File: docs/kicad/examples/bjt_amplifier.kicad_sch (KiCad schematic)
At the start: 18 parts, among them Q1 2N3904, Q2 2N3904

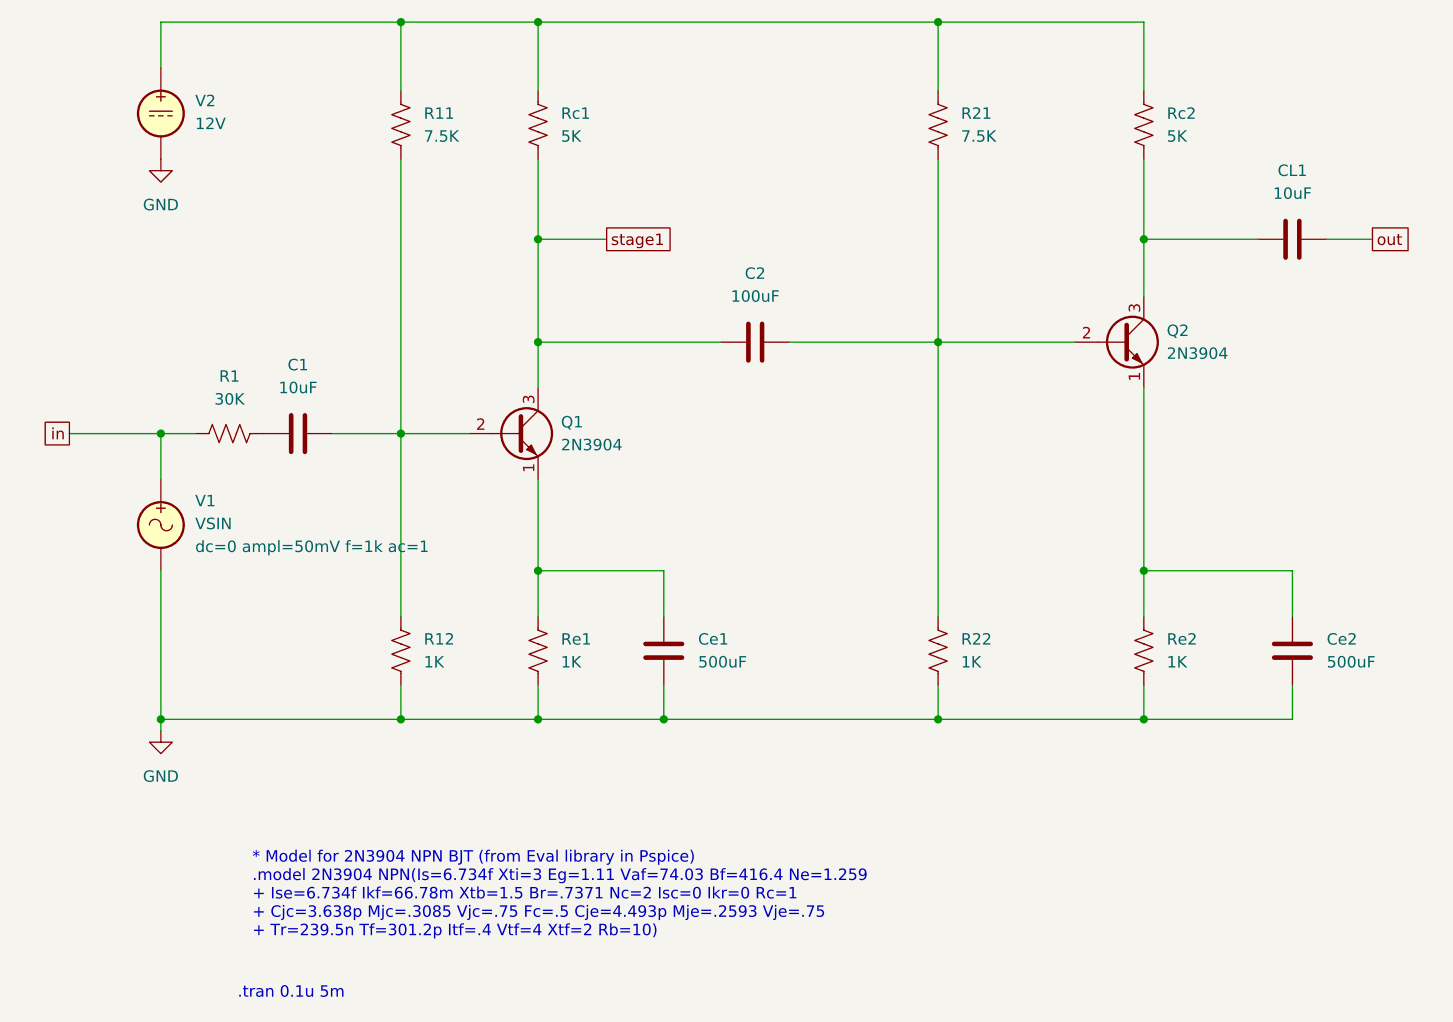
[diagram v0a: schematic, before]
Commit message: fix: file watcher polling, cross-probe removal, guide updates
- Rewrite file watcher from QFileSystemWatcher to mtime polling (KiCad's
  rename-over atomic save silently breaks QFileSystemWatcher tracking)
- Replace "Simulate Now" with "Re-Watch" button (resumes watching after Stop)
- Remove cross-probe/back-annotation from menu and docs (KiCad's cross-probe
  channel is private Eeschema-PcbNew, not an external API)
- Document cross-probe as known limitation in user guide
- Rename back_annotate.kicad_sch to bjt_amplifier.kicad_sch
- Make all Help dialogs non-modal (show() instead of exec())
- Add Help > KiCad User Guide entry with pre-built HTML
- Persist traces across KiCad re-simulations
- Add raw_ok check in bridge.simulate() (ngspice can exit 0 without writing .raw)
- Fix _panel_grid -> panel_grid typo in cross-probe helper
- Initialize all KiCad-related instance attributes

Co-Authored-By: Claude Opus 4.7 <noreply@anthropic.com>
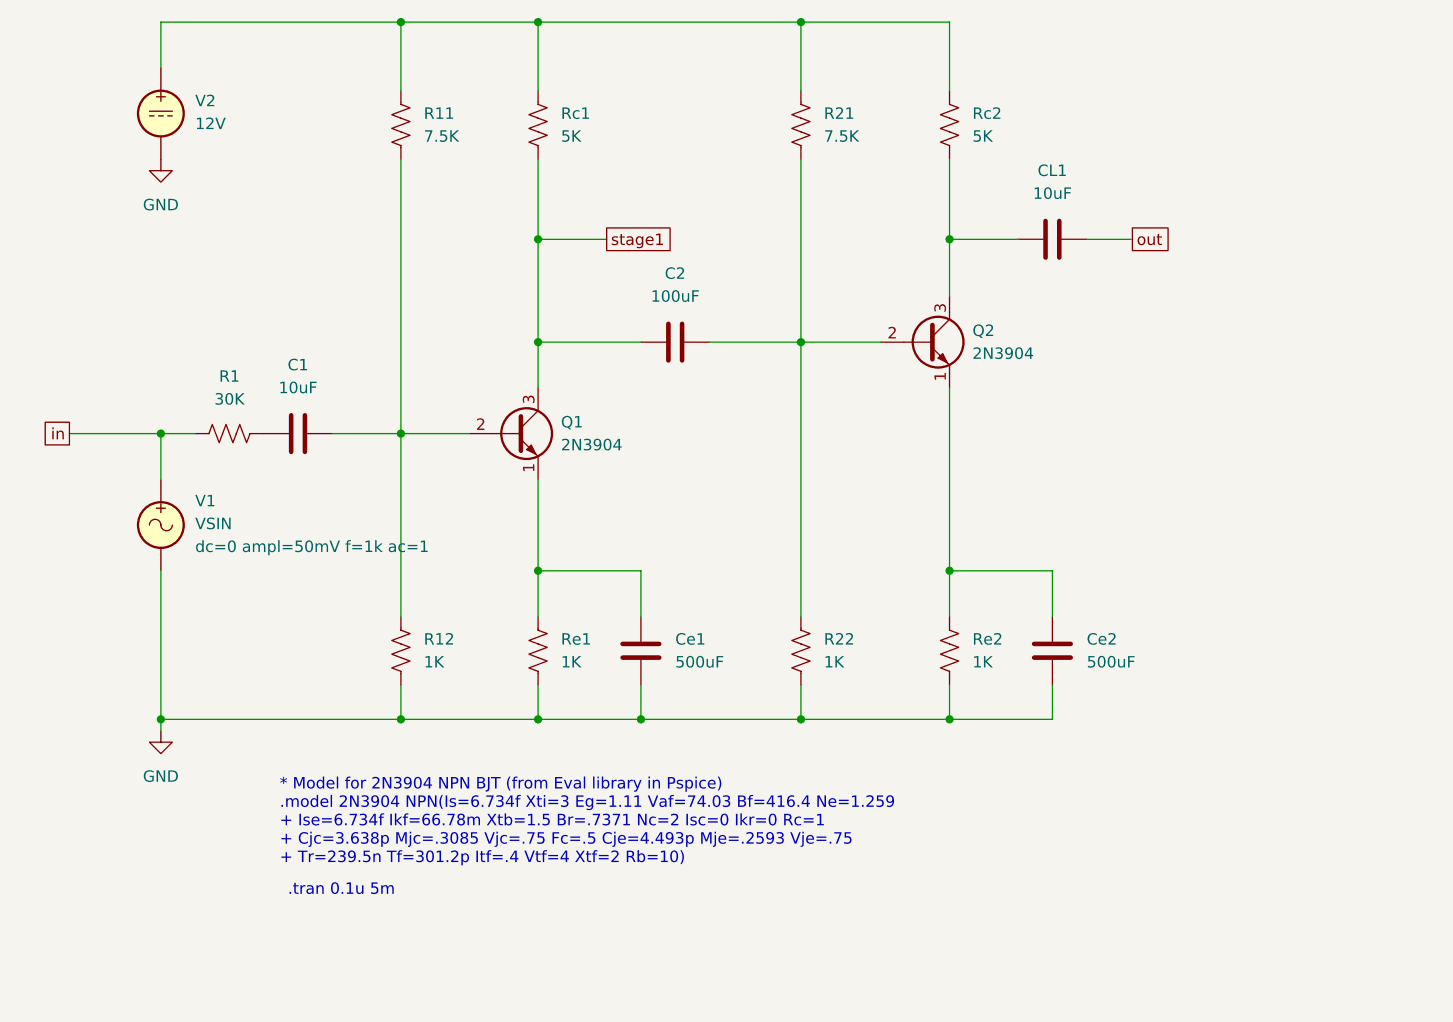
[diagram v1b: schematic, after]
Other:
- moved on the sheet: C2, CL1, Ce1, Ce2, Q2, R21, R22, Rc2, Re2
